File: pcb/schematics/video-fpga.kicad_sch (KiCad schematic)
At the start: 60 parts, among them J5 Conn_01x06, J6 Conn_01x06, U4 LCMXO2-7000HC-4TG144C, X1 ASV-xxxMHz

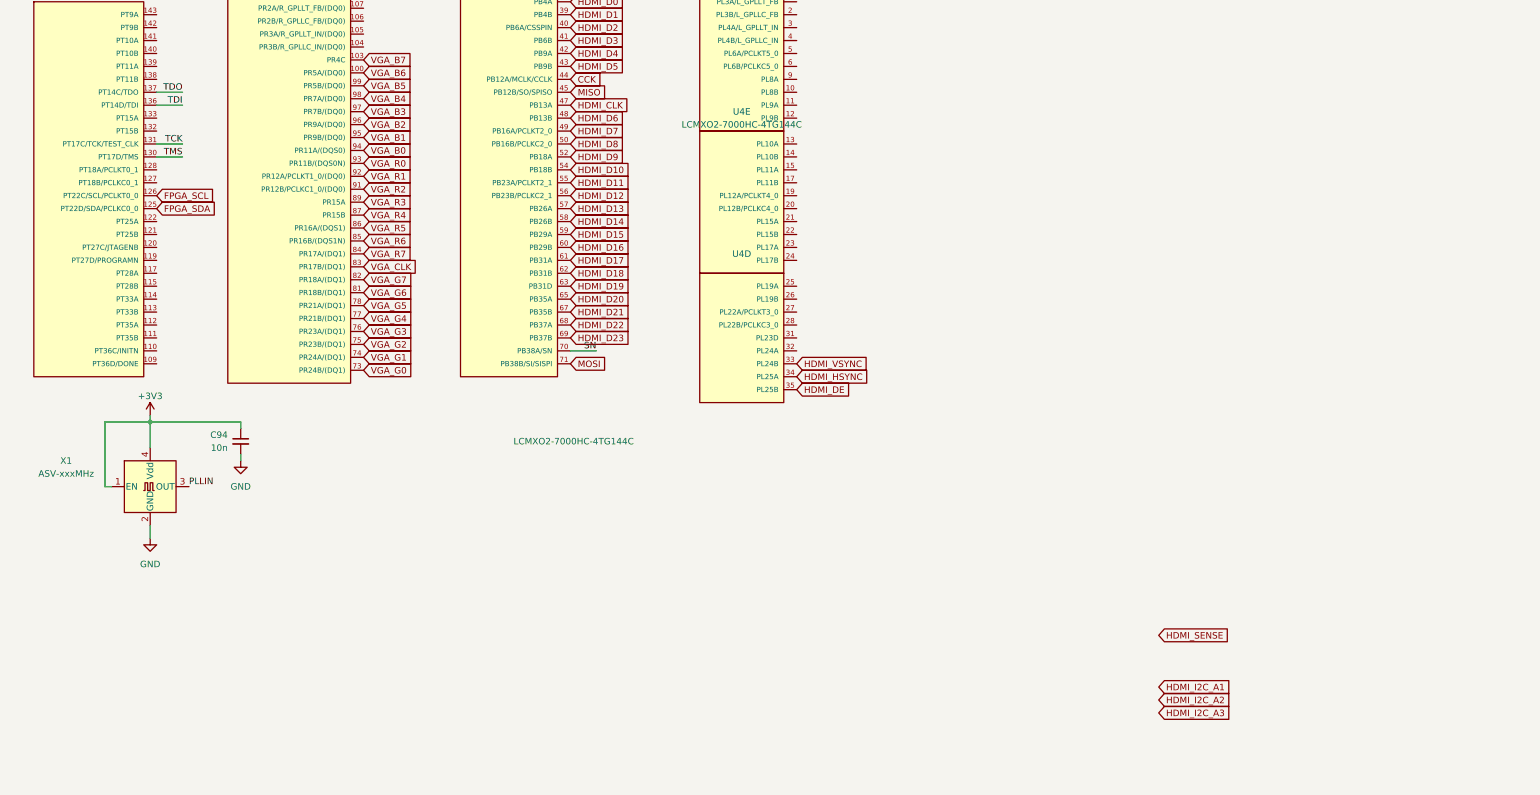
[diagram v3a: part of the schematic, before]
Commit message: add dualport ram for debug purposes
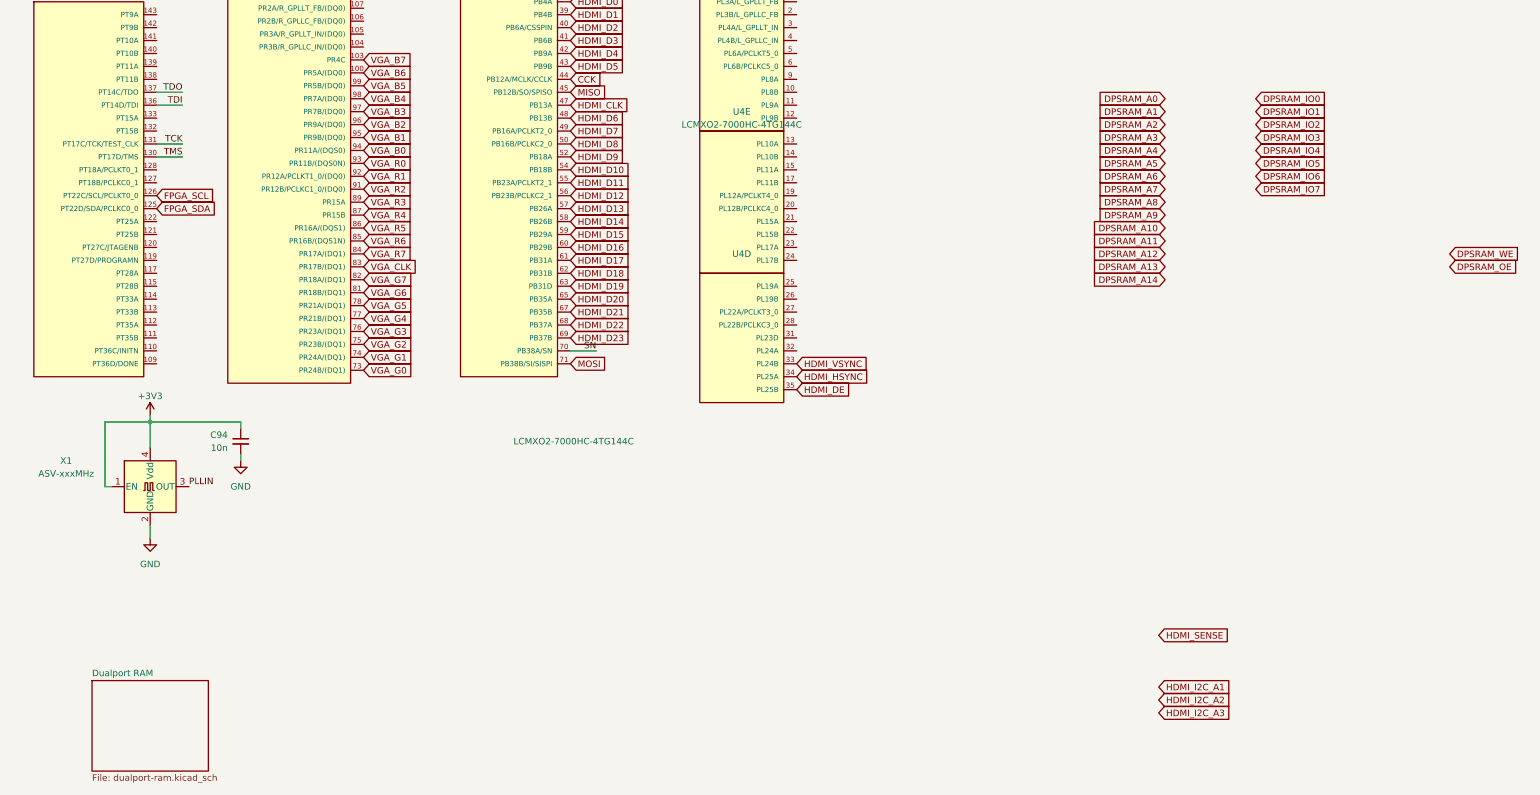
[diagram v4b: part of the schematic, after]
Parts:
- J5, J6: footprint Connector:Tag-Connect_TC2030-IDC-NL_2x03_P1.27mm_Vertical -> Connector:Tag-Connect_TC2030-IDC-FP_2x03_P1.27mm_Vertical
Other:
- added sheet Dualport RAM (dualport-ram.kicad_sch)

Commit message: route sram
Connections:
- net DPSRAM_A0: now also U4.21 (PL15A)
- net DPSRAM_A1: now also U4.20 (PL12B/PCLKC4_0)
- net DPSRAM_A10: now also U4.32 (PL24A)
- net DPSRAM_A11: now also U4.3 (PL4A/L_GPLLT_IN)
- net DPSRAM_A12: now also U4.11 (PL9A)
- net DPSRAM_A13: now also U4.6 (PL6B/PCLKC5_0)
- net DPSRAM_A14: now also U4.10 (PL8B)
- net DPSRAM_A2: now also U4.19 (PL12A/PCLKT4_0)
- net DPSRAM_A3: now also U4.17 (PL11B)
- net DPSRAM_A4: now also U4.15 (PL11A)
- net DPSRAM_A5: now also U4.14 (PL10B)
- net DPSRAM_A6: now also U4.13 (PL10A)
- net DPSRAM_A7: now also U4.12 (PL9B)
- net DPSRAM_A8: now also U4.5 (PL6A/PCLKT5_0)
- net DPSRAM_A9: now also U4.4 (PL4B/L_GPLLC_IN)
- net DPSRAM_IO0: now also U4.22 (PL15B)
- net DPSRAM_IO1: now also U4.23 (PL17A)
- net DPSRAM_IO2: now also U4.24 (PL17B)
- net DPSRAM_IO3: now also U4.25 (PL19A)
- net DPSRAM_IO4: now also U4.26 (PL19B)
- net DPSRAM_IO5: now also U4.27 (PL22A/PCLKT3_0)
- net DPSRAM_IO6: now also U4.28 (PL22B/PCLKC3_0)
- net DPSRAM_IO7: now also U4.31 (PL23D)
- net DPSRAM_OE: now also U4.2 (PL3B/L_GPLLC_FB)
- net DPSRAM_WE: now also U4.9 (PL8A)

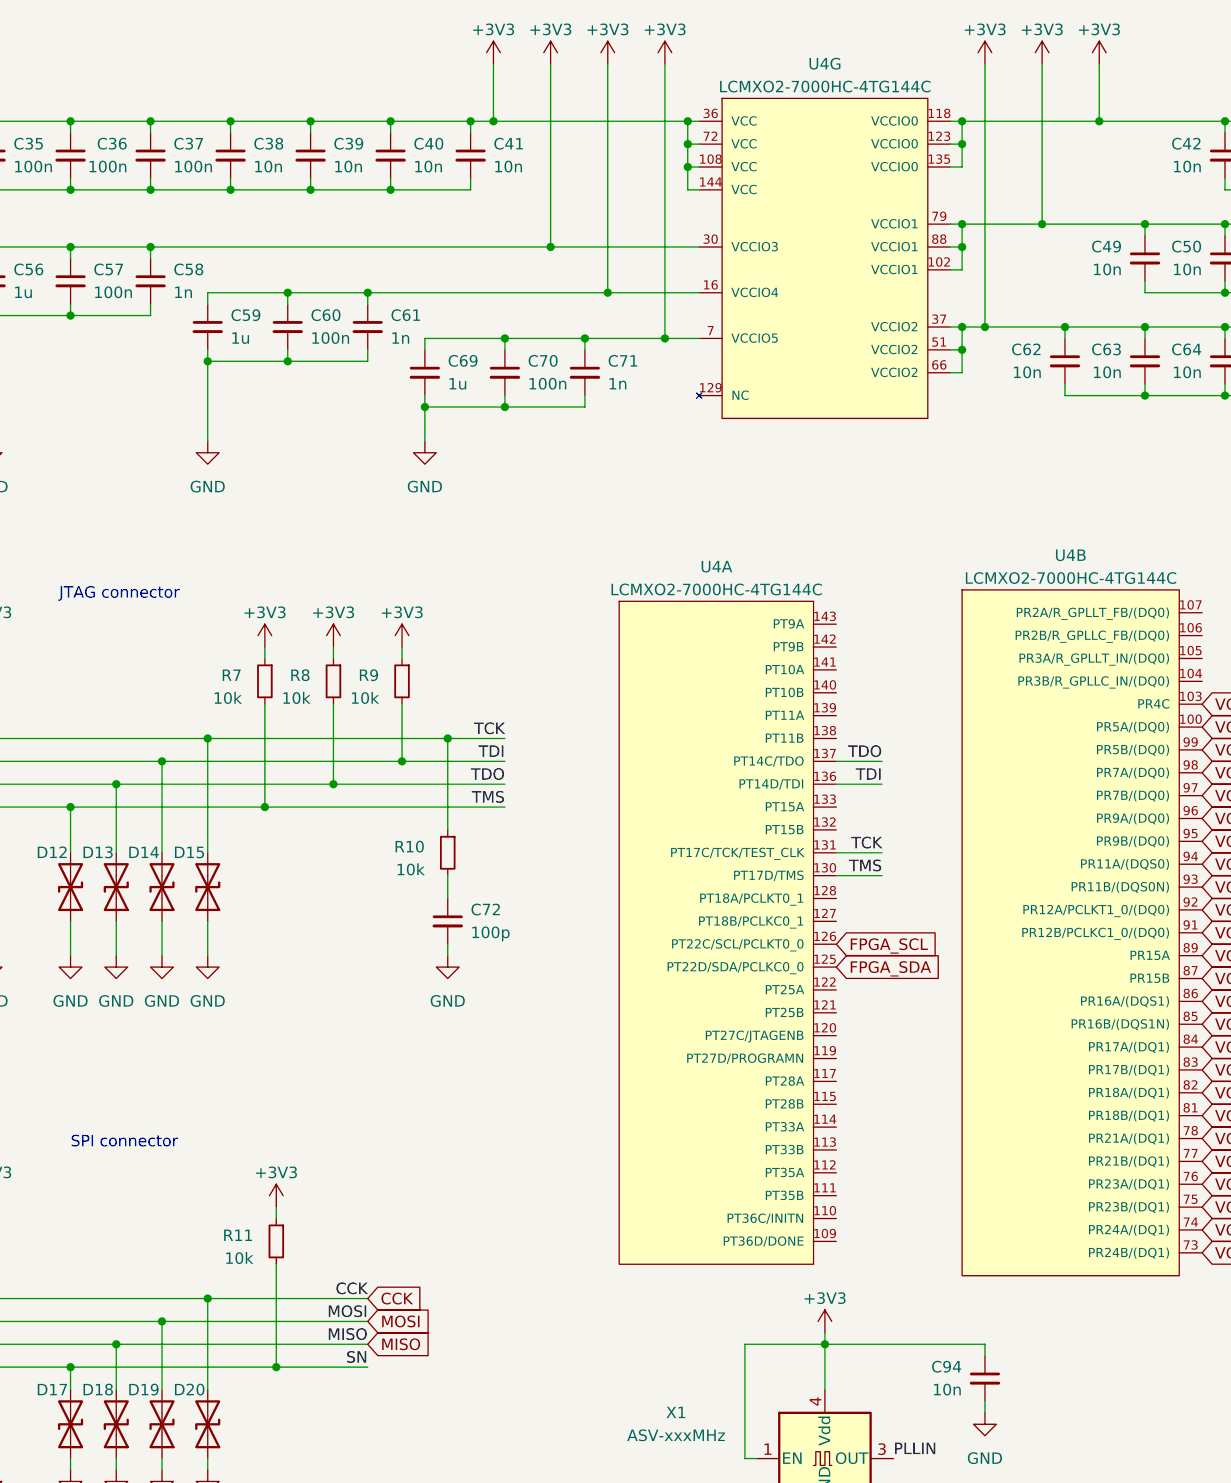
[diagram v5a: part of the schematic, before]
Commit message: add length matching to parallel buses
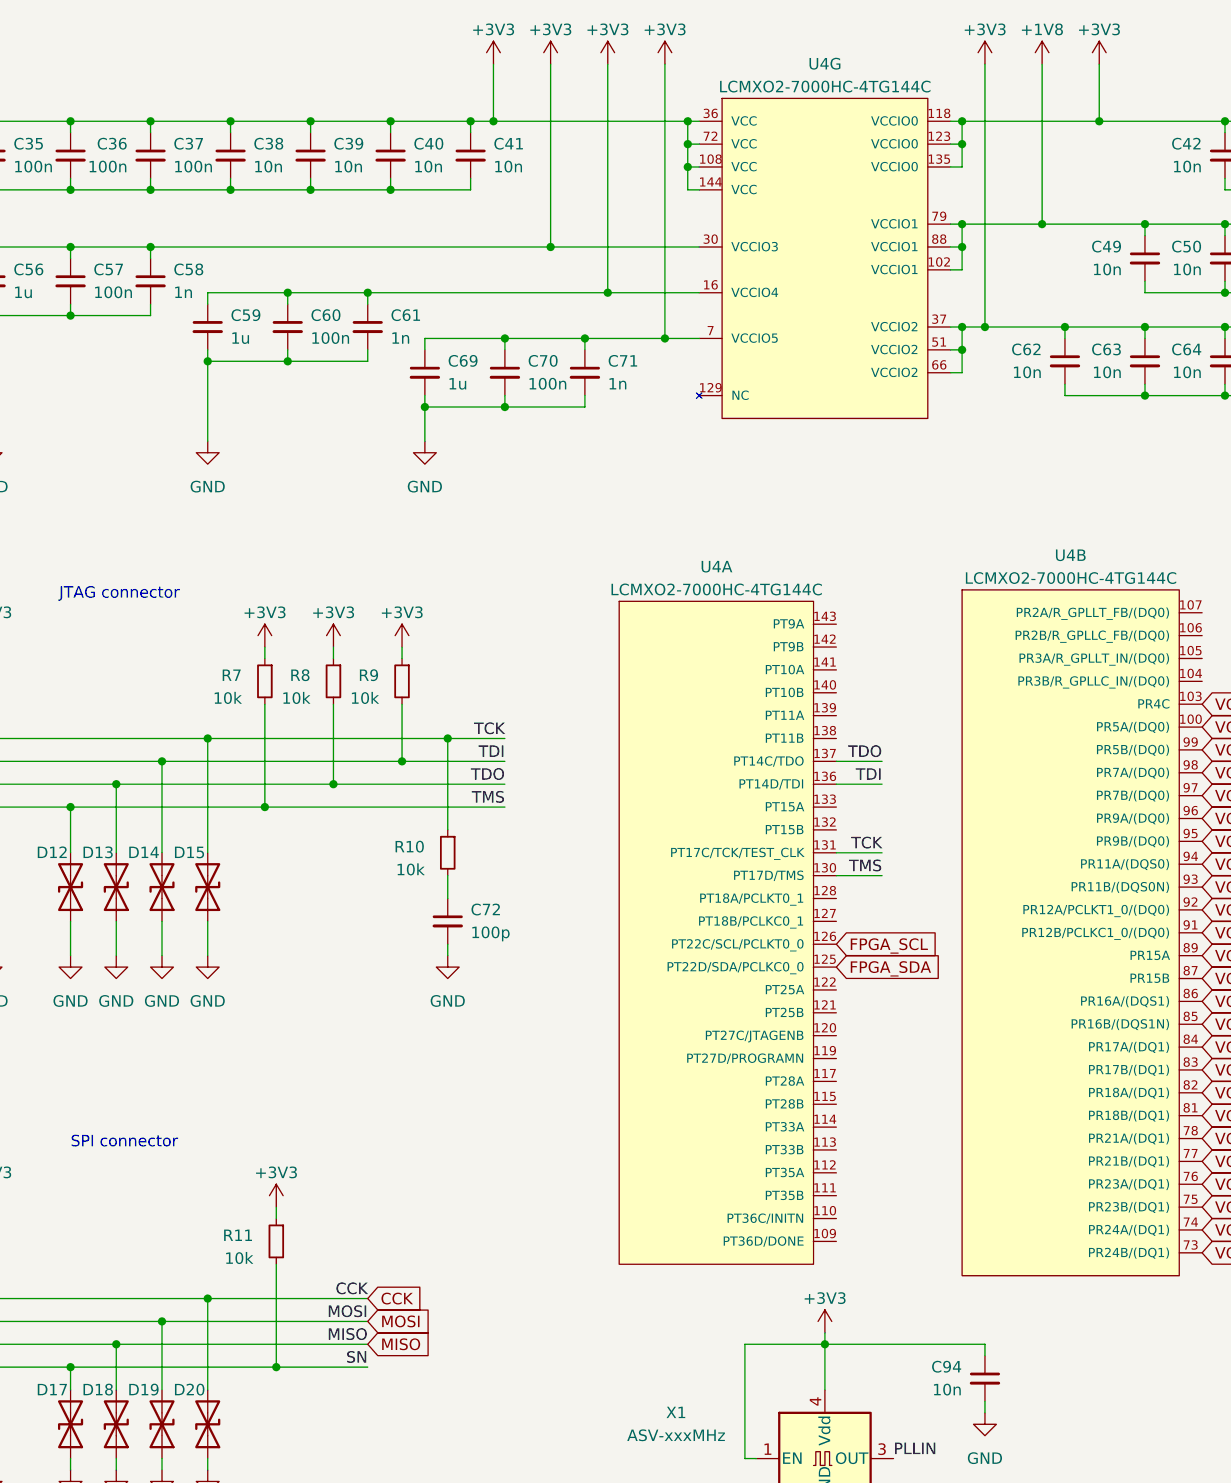
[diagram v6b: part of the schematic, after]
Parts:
- J5, J6: footprint Connector:Tag-Connect_TC2030-IDC-FP_2x03_P1.27mm_Vertical -> Connector:Tag-Connect_TC2030-IDC-NL_2x03_P1.27mm_Vertical
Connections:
- net +3V3: no longer C49.1, C50.1, C51.1, C52.1, C53.1, C54.1, C55.1, U4.102 (VCCIO1), U4.79 (VCCIO1), U4.88 (VCCIO1)
- new net +1V8: C49.1, C50.1, C51.1, C52.1, C53.1, C54.1, C55.1, U4.102 (VCCIO1), U4.79 (VCCIO1), U4.88 (VCCIO1)
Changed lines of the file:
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@@
   (junction (at 142.24 30.48) (diameter 0) (color 0 0 0 0)
   )
+  (junction (at 72.39 101.6) (diameter 0) (color 0 0 0 0)
+  )
   (junction (at 157.48 27.94) (diameter 0) (color 0 0 0 0)
   )
@@
   (junction (at 25.4 35.56) (diameter 0) (color 0 0 0 0)
   )
-  (junction (at 64.77 104.14) (diameter 0) (color 0 0 0 0)
-  )
   (junction (at 241.3 45.72) (diameter 0) (color 0 0 0 0)
   )
@@
   (junction (at 171.45 27.94) (diameter 0) (color 0 0 0 0)
   )
+  (junction (at 64.77 104.14) (diameter 0) (color 0 0 0 0)
+  )
   (junction (at 271.78 43.18) (diameter 0) (color 0 0 0 0)
   )
@@
   (junction (at 142.24 41.91) (diameter 0) (color 0 0 0 0)
   )
-  (junction (at 53.34 161.29) (diameter 0) (color 0 0 0 0)
-  )
   (junction (at 144.78 50.8) (diameter 0) (color 0 0 0 0)
   )
@@
   (junction (at 69.85 35.56) (diameter 0) (color 0 0 0 0)
   )
-  (junction (at 72.39 101.6) (diameter 0) (color 0 0 0 0)
-  )
   (junction (at 189.23 50.8) (diameter 0) (color 0 0 0 0)
   )
   (junction (at 25.4 27.94) (diameter 0) (color 0 0 0 0)
   )
-  (junction (at 80.01 99.06) (diameter 0) (color 0 0 0 0)
-  )
   (junction (at 127 163.83) (diameter 0) (color 0 0 0 0)
   )
@@
   (junction (at 58.42 158.75) (diameter 0) (color 0 0 0 0)
   )
+  (junction (at 85.09 96.52) (diameter 0) (color 0 0 0 0)
+  )
   (junction (at 153.67 50.8) (diameter 0) (color 0 0 0 0)
   )
@@
   (junction (at 66.04 166.37) (diameter 0) (color 0 0 0 0)
   )
+  (junction (at 80.01 99.06) (diameter 0) (color 0 0 0 0)
+  )
   (junction (at 78.74 27.94) (diameter 0) (color 0 0 0 0)
   )
-  (junction (at 224.79 35.56) (diameter 0) (color 0 0 0 0)
+  (junction (at 53.34 161.29) (diameter 0) (color 0 0 0 0)
   )
-  (junction (at 85.09 96.52) (diameter 0) (color 0 0 0 0)
+  (junction (at 224.79 35.56) (diameter 0) (color 0 0 0 0)
   )
   (junction (at 52.07 27.94) (diameter 0) (color 0 0 0 0)
@@
     (stroke (width 0) (type default))
   )
+  (wire (pts (xy 80.01 99.06) (xy 91.44 99.06))
+    (stroke (width 0) (type default))
+  )
   (wire (pts (xy 271.78 50.8) (xy 266.7 50.8))
     (stroke (width 0) (type default))
@@
     (stroke (width 0) (type default))
   )
-  (wire (pts (xy 85.09 96.52) (xy 91.44 96.52))
-    (stroke (width 0) (type default))
-  )
   (wire (pts (xy 198.12 27.94) (xy 207.01 27.94))
     (stroke (width 0) (type default))
@@
     (stroke (width 0) (type default))
   )
+  (wire (pts (xy 64.77 104.14) (xy 91.44 104.14))
+    (stroke (width 0) (type default))
+  )
   (wire (pts (xy 180.34 27.94) (xy 189.23 27.94))
     (stroke (width 0) (type default))
@@
     (stroke (width 0) (type default))
   )
+  (wire (pts (xy 72.39 101.6) (xy 91.44 101.6))
+    (stroke (width 0) (type default))
+  )
   (wire (pts (xy 21.59 110.49) (xy 34.29 110.49))
     (stroke (width 0) (type default))
@@
     (stroke (width 0) (type default))
   )
+  (wire (pts (xy 85.09 96.52) (xy 91.44 96.52))
+    (stroke (width 0) (type default))
+  )
   (wire (pts (xy 162.56 46.99) (xy 171.45 46.99))
     (stroke (width 0) (type default))
@@
     (stroke (width 0) (type default))
   )
-  (wire (pts (xy 80.01 99.06) (xy 91.44 99.06))
-    (stroke (width 0) (type default))
-  )
-  (wire (pts (xy 72.39 101.6) (xy 91.44 101.6))
-    (stroke (width 0) (type default))
-  )
   (wire (pts (xy 140.97 55.88) (xy 142.24 55.88))
     (stroke (width 0) (type default))
@@
     (stroke (width 0) (type default))
   )
+  (wire (pts (xy 53.34 161.29) (xy 76.2 161.29))
+    (stroke (width 0) (type default))
+  )
   (wire (pts (xy 90.17 21.59) (xy 90.17 27.94))
     (stroke (width 0) (type default))
@@
     (stroke (width 0) (type default))
   )
-  (wire (pts (xy 64.77 104.14) (xy 91.44 104.14))
-    (stroke (width 0) (type default))
-  )
   (wire (pts (xy 82.55 59.69) (xy 82.55 58.42))
     (stroke (width 0) (type default))
@@
     (stroke (width 0) (type default))
   )
-  (wire (pts (xy 76.2 161.29) (xy 53.34 161.29))
-    (stroke (width 0) (type default))
-  )
   (wire (pts (xy 111.76 30.48) (xy 111.76 33.02))
     (stroke (width 0) (type default))
@@
     (pin "1")
   )
+  (symbol (lib_id "power:+1V8") (at 151.13 21.59 0) (unit 1)
+    (in_bom yes) (on_board yes) (fields_autoplaced)
+    (property "Reference" "#PWR0111" (id 0) (at 151.13 25.4 0)
+      (effects (font (size 1.27 1.27)) hide)
+    )
+    (property "Value" "+1V8" (id 1) (at 151.13 17.78 0)
+      (effects (font (size 1.27 1.27)))
+    )
+    (property "Footprint" "" (id 2) (at 151.13 21.59 0)
+      (effects (font (size 1.27 1.27)) hide)
+    )
+    (property "Datasheet" "" (id 3) (at 151.13 21.59 0)
+      (effects (font (size 1.27 1.27)) hide)
+    )
+    (pin "1")
+  )
   (symbol (lib_id "power:GND") (at 58.42 177.8 0) (mirror y) (unit 1)
     (in_bom yes) (on_board yes) (fields_autoplaced)
@@
       (effects (font (size 1.27 1.27)) (justify left) hide)
     )
-    (property "Footprint" "Connector:Tag-Connect_TC2030-IDC-FP_2x03_P1.27mm_Vertical" (id 2) (at 27.94 161.29 0)
+    (property "Footprint" "Connector:Tag-Connect_TC2030-IDC-NL_2x03_P1.27mm_Vertical" (id 2) (at 27.94 161.29 0)
       (effects (font (size 1.27 1.27)) hide)
     )
@@
       (effects (font (size 1.27 1.27)) (justify left) hide)
     )
-    (property "Footprint" "Connector:Tag-Connect_TC2030-IDC-FP_2x03_P1.27mm_Vertical" (id 2) (at 27.94 99.06 0)
+    (property "Footprint" "Connector:Tag-Connect_TC2030-IDC-NL_2x03_P1.27mm_Vertical" (id 2) (at 27.94 99.06 0)
       (effects (font (size 1.27 1.27)) hide)
     )
@@
     (pin "2")
   )
-  (symbol (lib_id "power:+3V3") (at 151.13 21.59 0) (unit 1)
-    (in_bom yes) (on_board yes) (fields_autoplaced)
-    (property "Reference" "#PWR046" (id 0) (at 151.13 25.4 0)
-      (effects (font (size 1.27 1.27)) hide)
-    )
-    (property "Value" "+3V3" (id 1) (at 151.13 17.78 0)
-      (effects (font (size 1.27 1.27)))
-    )
-    (property "Footprint" "" (id 2) (at 151.13 21.59 0)
-      (effects (font (size 1.27 1.27)) hide)
-    )
-    (property "Datasheet" "" (id 3) (at 151.13 21.59 0)
-      (effects (font (size 1.27 1.27)) hide)
-    )
-    (pin "1")
-  )
   (sheet (at 115.57 214.63) (size 22.86 17.78) (fields_autoplaced)
